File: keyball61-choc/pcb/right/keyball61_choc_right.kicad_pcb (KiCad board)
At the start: 2 copper layers, 143.3 x 107.5 mm, 138 parts, among them J1 OLED, J13 TRS_JACK, J2 BALL_PCB, J3 Conn_01x01-Connector_Generic, J4 Conn_01x01-Connector_Generic, P1 I2C, P2 I2C, SW1 Choc_V1, SW10 Choc_V1, SW11 Choc_V1, SW12 Choc_V1, SW13 Choc_V1, SW14 Choc_V1, SW15 Choc_V1, SW16 Choc_V1, SW17 Choc_V1, SW18 Choc_V1, SW19 Choc_V1, SW2 Choc_V1, SW20 Choc_V1, SW21 Choc_V1, SW22 Choc_V1, SW23 Choc_V1, SW24 Choc_V1, SW25 Choc_V1, SW26 Choc_V1, SW27 Choc_V1, SW28 Choc_V1, SW29 Choc_V1, SW3 Choc_V1, SW30 RESET_SW, SW4 Choc_V1, SW5 Choc_V1, SW6 Choc_V1, SW7 Choc_V1, SW8 Choc_V1, SW9 Choc_V1, U1 ProMicro-kbd

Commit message: WIP: routed boards from previous run (DRC: L 4 err/3 open, R 10 err/8 open)
Superseded by the routing run in progress.

Co-Authored-By: Claude Opus 5.5 <noreply@anthropic.com>
Claude-Session: https://claude.ai/code/session_012Lz4SD3XgX9T3cBqnotnnt
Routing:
- net NCS: track 138.7 -> 20.6 mm, vias 5 -> 2
- net Net-(LED7-Pad2): track 0.00 -> 85.7 mm, vias 0 -> 2
- net Net-(LED29-Pad2): track 0.00 -> 81.7 mm, vias 0 -> 4
- net GND: track 632.3 -> 702.0 mm, vias 28 -> 8
- net ROW3: track 151.2 -> 175.0 mm, vias 5 -> 6
- net Net-(D29-Pad1): track 20.1 -> 0.00 mm
- net COL0: track 198.0 -> 217.7 mm, vias 7 -> 6
- net MOSI: track 141.2 -> 124.6 mm, vias 6 -> 2
- net Net-(LED12-Pad2): track 111.7 -> 96.4 mm
- net Net-(LED25-Pad2): track 61.1 -> 76.4 mm
- net Net-(D28-Pad1): track 24.0 -> 37.2 mm
- net VCC: track 197.3 -> 185.0 mm, vias 0 -> 1
- net ROW1: track 139.6 -> 127.8 mm
- net Net-(D4-Pad1): track 31.8 -> 20.3 mm
- net Net-(LED8-Pad2): track 18.6 -> 29.3 mm, vias 0 -> 2
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
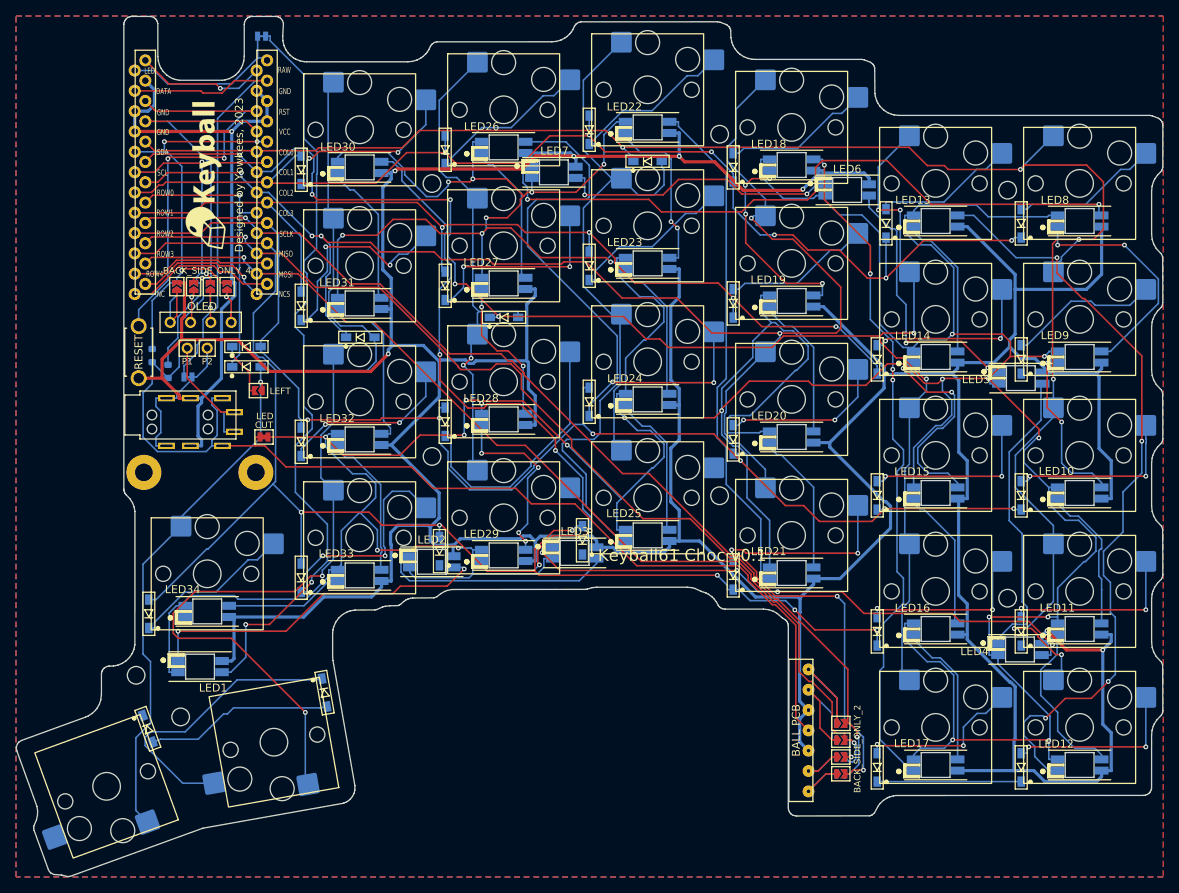
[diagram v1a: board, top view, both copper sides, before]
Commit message: WIP: boards from previous routing run (DRC: L 14 err/2 open, R 28 err/6 open)
Superseded by the iterative routing run in progress.

Co-Authored-By: Claude Opus 5.5 <noreply@anthropic.com>
Claude-Session: https://claude.ai/code/session_012Lz4SD3XgX9T3cBqnotnnt
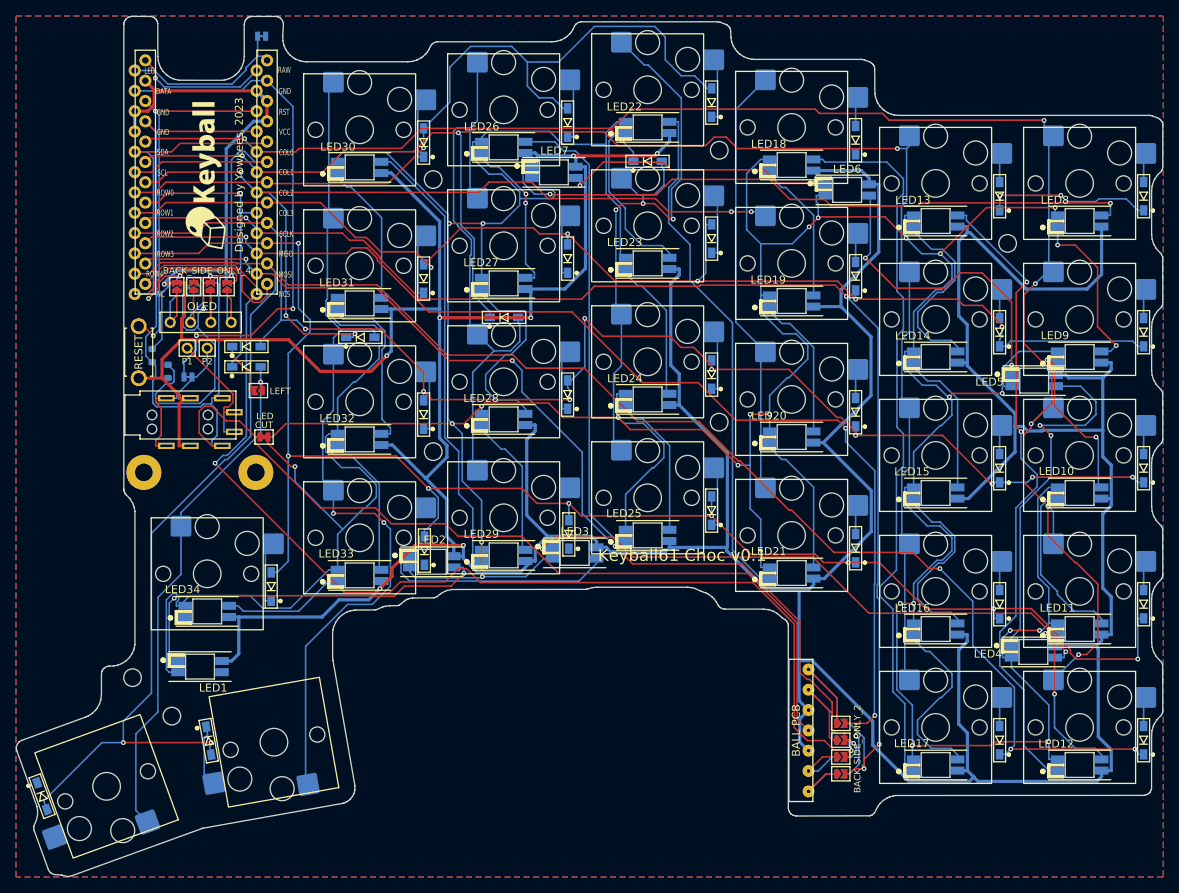
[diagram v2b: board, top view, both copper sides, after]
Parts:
- removed MH10: M2, keyball61_choc:MountingHole_2.2mm_M2
- moved D22 16.6 mm to (166.2, 105.1)
- moved D23 16.3 mm to (148.3, 108.0)
- moved D24 15.8 mm to (130.3, 110.1)
- moved D11 15.7 mm to (148.2, 73.6)
- moved D17 15.7 mm to (148.2, 90.6)
- moved D5 15.7 mm to (148.2, 56.6)
- moved D28 15.7 mm to (103.3, 133.8)
- moved D29 15.7 mm to (82.5, 140.8)
- moved D26 15.7 mm to (220.2, 133.8)
- moved D27 15.7 mm to (202.2, 133.8)
- moved D25 15.7 mm to (111.1, 114.6)
- moved D6 15.7 mm to (130.2, 59.1)
- moved D12 15.7 mm to (130.2, 76.1)
- moved D18 15.7 mm to (130.2, 93.1)
- moved D19 15.7 mm to (220.2, 116.8)
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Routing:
- net ROW4: track 59.9 -> 258.1 mm, vias 0 -> 5
- net NCS: track 20.6 -> 149.8 mm
- net Net-(JP20-Pad2): track 95.2 -> 0.00 mm, vias 2 -> 0
- net SCL: track 47.4 -> 82.6 mm
- net Net-(JP19-Pad1): track 672.8 -> 639.7 mm, vias 26 -> 24
- net SCLK: track 133.4 -> 165.5 mm, vias 3 -> 4
- net ROW3: track 175.0 -> 204.2 mm, vias 6 -> 8
- net Net-(D28-Pad1): track 37.2 -> 8.31 mm
- net Net-(D24-Pad1): track 27.5 -> 0.00 mm, vias 2 -> 0
- net Net-(LED29-Pad2): track 81.7 -> 56.4 mm, vias 4 -> 0
- net ROW1: track 127.8 -> 152.9 mm, vias 4 -> 5
- net Net-(D17-Pad1): track 33.0 -> 8.27 mm
- net GND: track 702.0 -> 724.3 mm
- net Net-(D33-Pad2): track 128.3 -> 108.5 mm
- net Net-(D21-Pad2): track 23.4 -> 3.69 mm, vias 2 -> 0
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
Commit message: Iteratively routed boards (0 DRC violations; L 2 / R 7 open) + fixup.py grid router with rip-up
Co-Authored-By: Claude Opus 5.5 <noreply@anthropic.com>
Claude-Session: https://claude.ai/code/session_012Lz4SD3XgX9T3cBqnotnnt
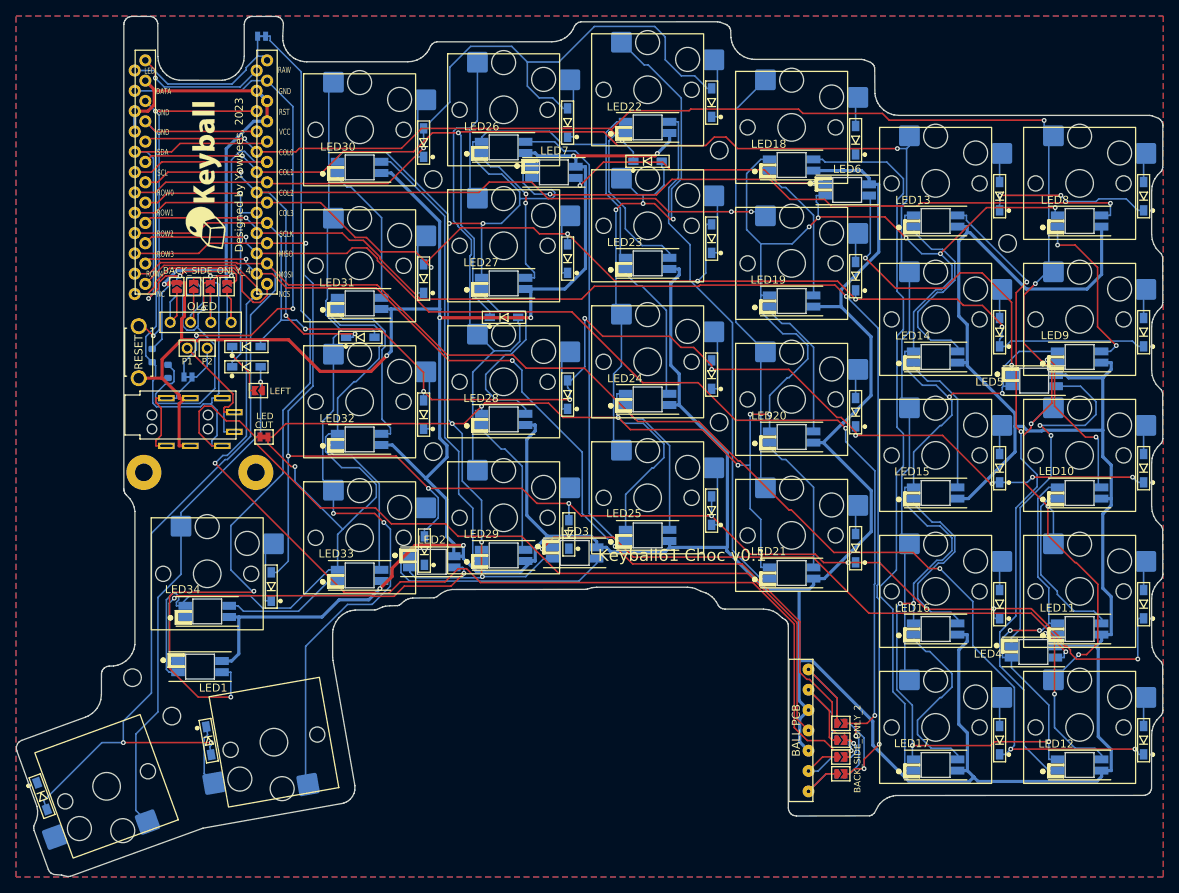
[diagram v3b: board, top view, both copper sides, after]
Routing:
- net Net-(JP20-Pad2): track 0.00 -> 110.6 mm, vias 0 -> 2
- net Net-(J1-Pad2): track 14.7 -> 12.9 mm
- net SCL: track 82.6 -> 80.9 mm
- net ROW3: track 204.2 -> 205.3 mm

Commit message: Keyball61 Choc v0.1: DRC-clean routed PCBs, JLC fab files, bottom plates, renders
Both halves: 0 DRC errors, 0 unconnected (KiCad 9). Gerbers + drill,
JLC BOM/CPL (single-sided assembly), 2 mm acrylic bottom plates with the
original trackball-case holes, and 3D renders. Docs updated.

Co-Authored-By: Claude Opus 5.5 <noreply@anthropic.com>
Claude-Session: https://claude.ai/code/session_012Lz4SD3XgX9T3cBqnotnnt
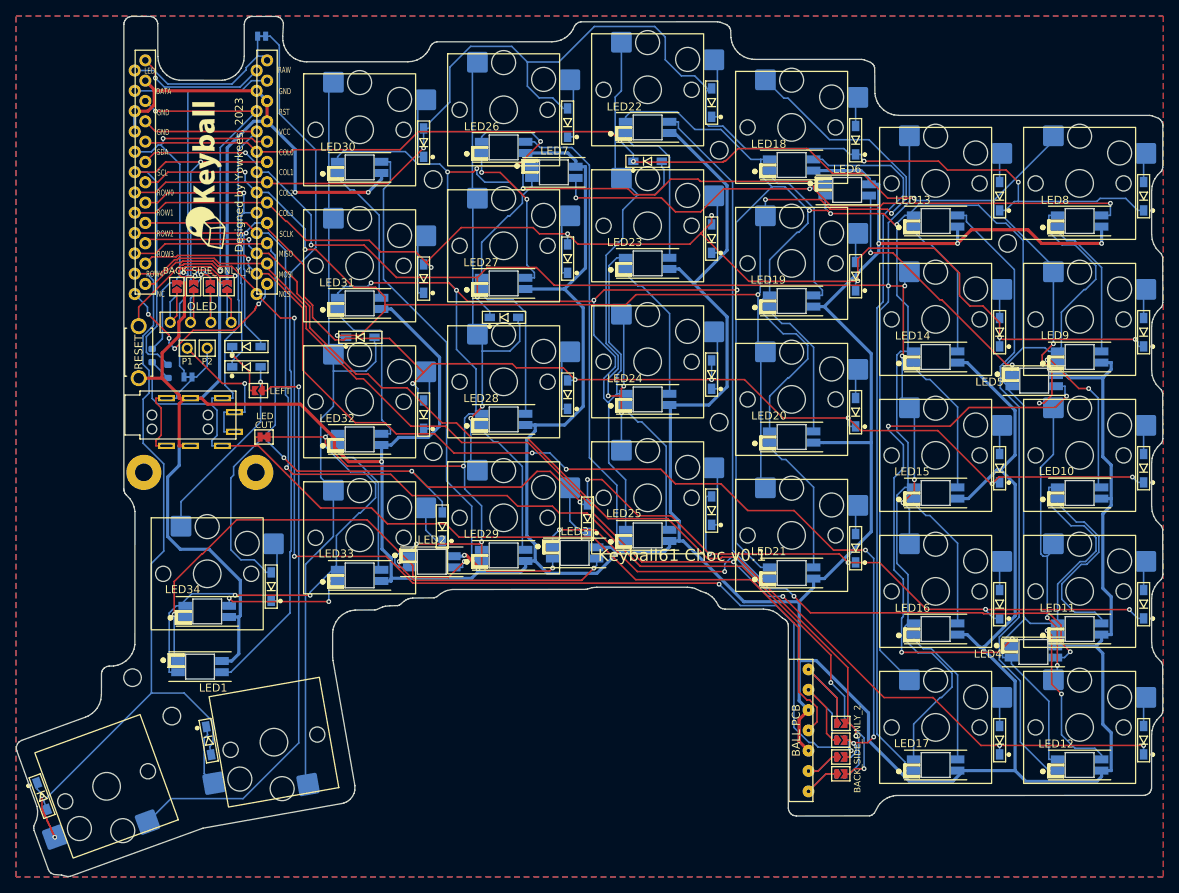
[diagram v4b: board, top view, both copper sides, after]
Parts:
- moved D24 3.74 mm to (132.5, 107.1)
- moved D23 3.05 mm to (150.6, 106.1)
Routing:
- net Net-(JP19-Pad1): track 639.7 -> 689.8 mm, vias 24 -> 17
- net ROW0: track 122.8 -> 169.8 mm
- net Net-(D34-Pad2): track 65.1 -> 97.5 mm, vias 1 -> 2
- net GND: track 724.3 -> 756.5 mm
- net Net-(LED4-Pad2): track 45.8 -> 71.9 mm, vias 2 -> 4
- net COL1: track 196.1 -> 218.7 mm, vias 3 -> 8
- net Net-(JP20-Pad2): track 110.6 -> 88.1 mm, vias 2 -> 0
- net SCLK: track 165.5 -> 143.1 mm, vias 4 -> 3
- net MISO: track 148.1 -> 128.7 mm, vias 4 -> 2
- net COL0: track 213.0 -> 195.8 mm
- net SCL: track 80.9 -> 64.9 mm
- net DATA: track 66.2 -> 53.5 mm, vias 2 -> 0
- net COL2: track 165.7 -> 178.1 mm, vias 5 -> 6
- net MOSI: track 129.3 -> 141.5 mm, vias 4 -> 6
- net Net-(D32-Pad2): track 73.1 -> 61.4 mm, vias 0 -> 2
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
